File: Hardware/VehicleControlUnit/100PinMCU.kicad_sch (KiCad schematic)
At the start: 28 parts, among them J1 SWD_Header_02x02, U2 STM32G491VET6_1, Y1 Crystal

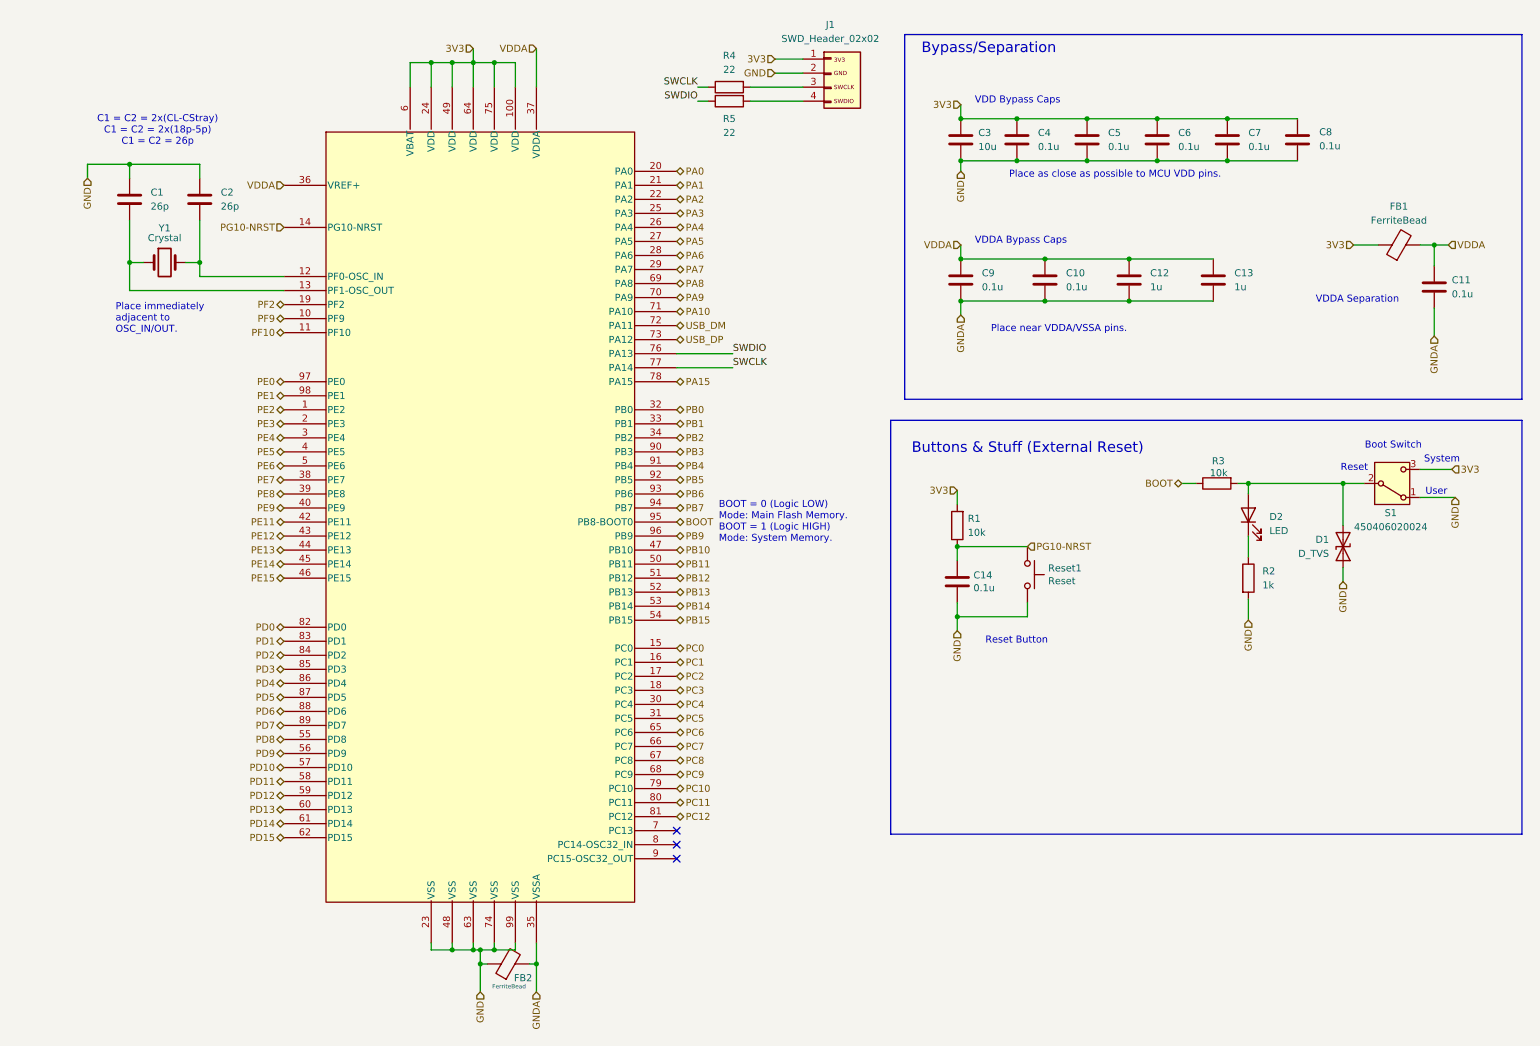
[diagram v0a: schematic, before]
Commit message: mcu pinouts todo - peripherals done
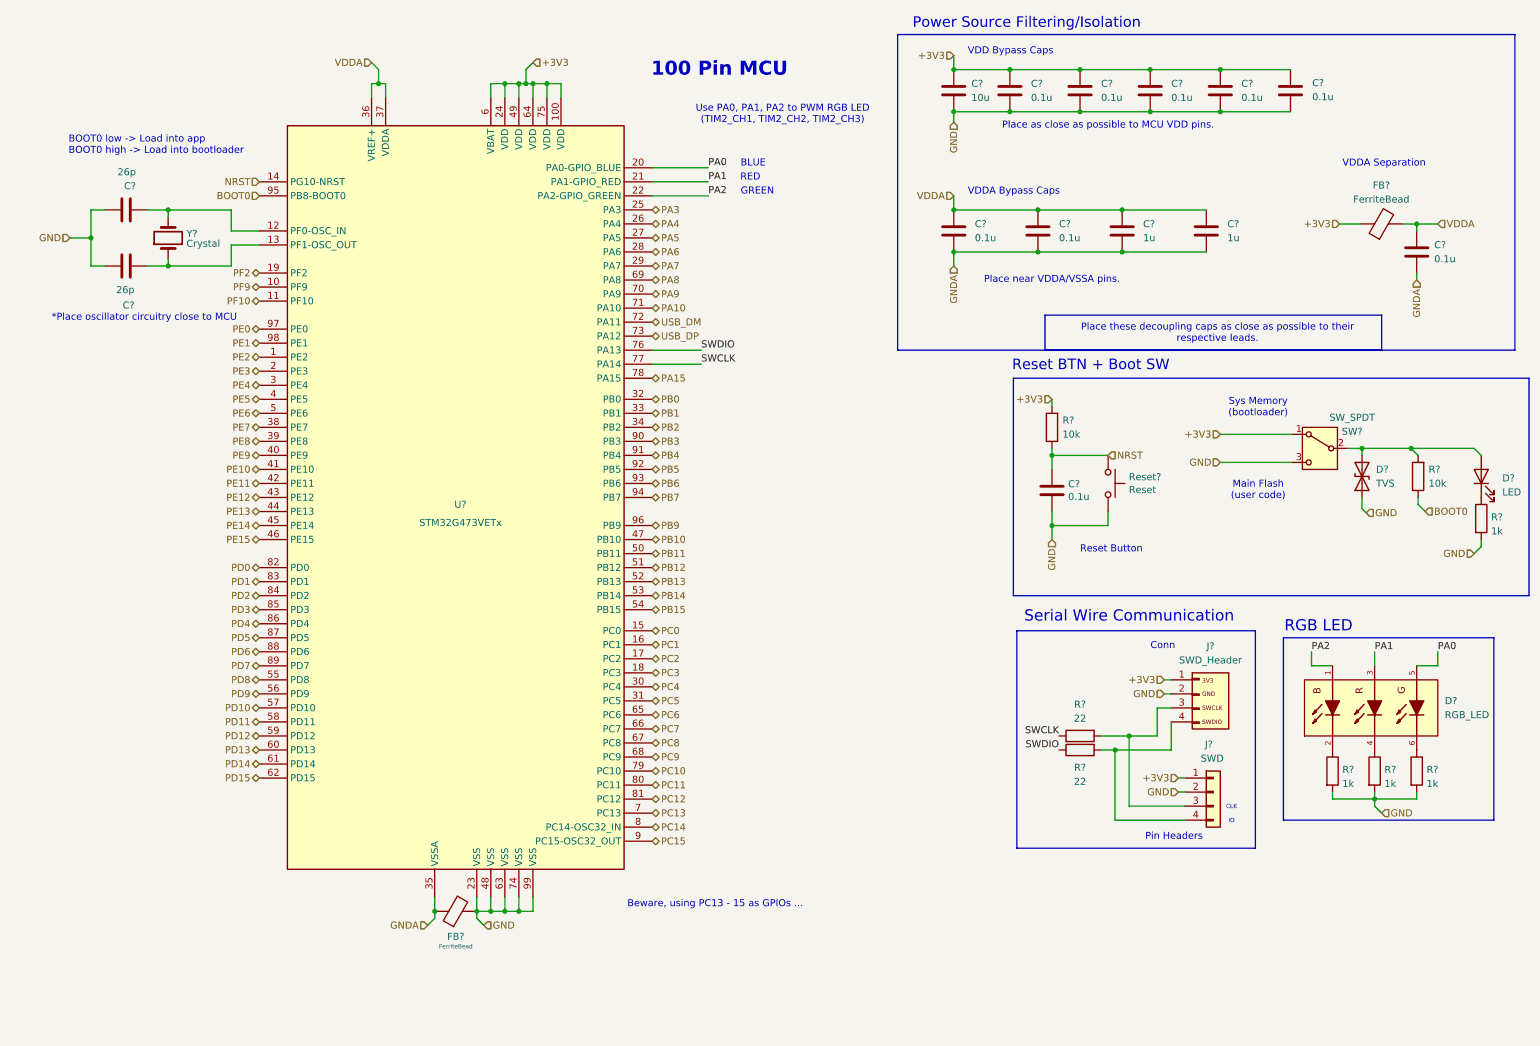
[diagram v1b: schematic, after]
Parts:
- removed C1, C2: 26p, Capacitor_SMD:C_0603_1608Metric_Pad1.08x0.95mm_HandSolder, symbol Device:C
- removed D1: D_TVS, Diode_SMD:D_SOD-323, symbol Device:D_TVS
- removed D2: LED, LED_SMD:LED_0201_0603Metric, symbol Device:LED
- removed FB2: FerriteBead, Capacitor_SMD:C_0603_1608Metric_Pad1.08x0.95mm_HandSolder, symbol Device:FerriteBead
- removed R2: 1k, Resistor_SMD:R_0603_1608Metric_Pad0.98x0.95mm_HandSolder, symbol Device:R
- removed R3: 10k, Resistor_SMD:R_0603_1608Metric_Pad0.98x0.95mm_HandSolder, symbol Device:R
- removed R4, R5: 22, Resistor_SMD:R_0603_1608Metric_Pad0.98x0.95mm_HandSolder, symbol Device:R
- removed S1: 450406020024, LHRS_Special:BootSW, symbol Switch:SW_SPDT
- removed U2: STM32G491VET6_1, LHRS_ICs:LQFP_491VET6_STM, symbol lhrs_ics:STM32G491VET6_1
- removed Y1: Crystal, LHRS_Passives:Crystal_SMD_Abracon_ABM3-2Pin_5.0x3.2mm, symbol Device:Crystal
- added C? (x2): 26p, Capacitor_SMD:C_0603_1608Metric_Pad1.08x0.95mm_HandSolder, symbol Device:C
- added D?: LED, LED_SMD:LED_0603_1608Metric, symbol lhrs_misc:Blue_LED
- added D?: TVS, Diode_SMD:D_SOD-323, symbol lhrs_misc:Boot_TVS
- added D?: RGB_LED, LHRS_Special:RGB_LED, symbol lhrs_special:RGB_LED
- added FB?: FerriteBead, Capacitor_SMD:C_0603_1608Metric_Pad1.08x0.95mm_HandSolder, symbol Device:FerriteBead
- added J?: SWD, Connector_PinHeader_2.54mm:PinHeader_1x04_P2.54mm_Vertical, symbol Connector_Generic:Conn_01x04
- added R? (x4): 1k, Resistor_SMD:R_0603_1608Metric_Pad0.98x0.95mm_HandSolder, symbol Device:R
- added R? (x2): 22, Resistor_SMD:R_0603_1608Metric_Pad0.98x0.95mm_HandSolder, symbol Device:R
- added R?: 10k, Resistor_SMD:R_0603_1608Metric_Pad0.98x0.95mm_HandSolder, symbol Device:R
- added SW?: SW_SPDT, LHRS_Special:BootSW, symbol Switch:SW_SPDT
- added U?: STM32G473VETx, LHRS_Special:100PinMCU, symbol lhrs_special:STM32G473VET6
- added Y?: Crystal, LHRS_Passives:Crystal_SMD_Abracon_ABM3-2Pin_5.0x3.2mm, symbol Device:Crystal
- J?: renamed from J1; value SWD_Header_02x02 -> SWD_Header
- renumbered C12 to C?, C10 to C?, C4 to C?, C9 to C?, C6 to C?, C7 to C?, C3 to C?, C13 to C?, C14 to C?, C11 to C?, C5 to C?, C8 to C?, FB1 to FB?, R1 to R?, Reset1 to Reset?
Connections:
- net GND: now also C?.1, C?.1, D?.1 (A1), FB?.2, J?.2 (Pin_2), R?.2, R?.2, R?.2, R?.2, SW?.3 (C), U?.23 (VSS), U?.48 (VSS), U?.63 (VSS), U?.74 (VSS), U?.99 (VSS)
- net GNDA: now also FB?.1, U?.35 (VSSA)
- net PA0: now also D?.5, U?.20 (PA0-GPIO_BLUE)
- net PA1: now also D?.3, U?.21 (PA1-GPIO_RED)
- net PA10: now also U?.71 (PA10)
- net PA15: now also U?.78 (PA15)
- net PA2: now also D?.1, U?.22 (PA2-GPIO_GREEN)
- net PA3: now also U?.25 (PA3)
- net PA4: now also U?.26 (PA4)
- net PA5: now also U?.27 (PA5)
- net PA6: now also U?.28 (PA6)
- net PA7: now also U?.29 (PA7)
- net PA8: now also U?.69 (PA8)
- net PA9: now also U?.70 (PA9)
- net PB0: now also U?.32 (PB0)
- net PB1: now also U?.33 (PB1)
- net PB10: now also U?.47 (PB10)
- net PB11: now also U?.50 (PB11)
- net PB12: now also U?.51 (PB12)
- net PB13: now also U?.52 (PB13)
- net PB14: now also U?.53 (PB14)
- net PB15: now also U?.54 (PB15)
- net PB2: now also U?.34 (PB2)
- net PB3: now also U?.90 (PB3)
- net PB4: now also U?.91 (PB4)
- net PB5: now also U?.92 (PB5)
- net PB6: now also U?.93 (PB6)
- net PB7: now also U?.94 (PB7)
- net PB9: now also U?.96 (PB9)
- net PC0: now also U?.15 (PC0)
- net PC1: now also U?.16 (PC1)
- net PC10: now also U?.79 (PC10)
- net PC11: now also U?.80 (PC11)
- net PC12: now also U?.81 (PC12)
- net PC2: now also U?.17 (PC2)
- net PC3: now also U?.18 (PC3)
- net PC4: now also U?.30 (PC4)
- net PC5: now also U?.31 (PC5)
- net PC6: now also U?.65 (PC6)
- net PC7: now also U?.66 (PC7)
- net PC8: now also U?.67 (PC8)
- net PC9: now also U?.68 (PC9)
- net PD0: now also U?.82 (PD0)
- net PD1: now also U?.83 (PD1)
- net PD10: now also U?.57 (PD10)
- net PD11: now also U?.58 (PD11)
- net PD12: now also U?.59 (PD12)
- net PD13: now also U?.60 (PD13)
- net PD14: now also U?.61 (PD14)
- net PD15: now also U?.62 (PD15)
- net PD2: now also U?.84 (PD2)
- net PD3: now also U?.85 (PD3)
- net PD4: now also U?.86 (PD4)
- net PD5: now also U?.87 (PD5)
- net PD6: now also U?.88 (PD6)
- net PD7: now also U?.89 (PD7)
- net PD8: now also U?.55 (PD8)
- net PD9: now also U?.56 (PD9)
- net PE0: now also U?.97 (PE0)
- net PE1: now also U?.98 (PE1)
- net PE11: now also U?.42 (PE11)
- net PE12: now also U?.43 (PE12)
- net PE13: now also U?.44 (PE13)
- net PE14: now also U?.45 (PE14)
- net PE15: now also U?.46 (PE15)
- net PE2: now also U?.1 (PE2)
- net PE3: now also U?.2 (PE3)
- net PE4: now also U?.3 (PE4)
- net PE5: now also U?.4 (PE5)
- net PE6: now also U?.5 (PE6)
- net PE7: now also U?.38 (PE7)
- net PE8: now also U?.39 (PE8)
- net PE9: now also U?.40 (PE9)
- net PF10: now also U?.11 (PF10)
- net PF2: now also U?.19 (PF2)
- net PF9: now also U?.10 (PF9)
- net SWCLK: now also R?.1, U?.77 (PA14)
- net SWDIO: now also R?.1, U?.76 (PA13)
- net USB_DM: now also U?.72 (PA11)
- net USB_DP: now also U?.73 (PA12)
- net VDDA: now also U?.36 (VREF+), U?.37 (VDDA)
- net at J?.3 (Pin_3): now also J?.3 (Pin_3), R?.2
- net at J?.4 (Pin_4): now also J?.4 (Pin_4), R?.2
- net 3V3 renamed +3V3
- net +3V3: now also J?.1 (Pin_1), SW?.1 (A), U?.100 (VDD), U?.24 (VDD), U?.49 (VDD), U?.6 (VBAT), U?.64 (VDD), U?.75 (VDD)
- net PG10-NRST renamed NRST
- net NRST: now also U?.14 (PG10-NRST)
- new net: D?.1 (K), R?.1
- new net: D?.2 (A), D?.2 (A2), R?.2, SW?.2 (B)
- new net: C?.2, U?.12 (PF0-OSC_IN), Y?.2
- new net: C?.2, U?.13 (PF1-OSC_OUT), Y?.1
- new net: D?.2, R?.1
- new net: D?.4, R?.1
- new net: D?.6, R?.1
- new net BOOT0: R?.1, U?.95 (PB8-BOOT0)
- new net PC13: U?.7 (PC13)
- new net PC14: U?.8 (PC14-OSC32_IN)
- new net PC15: U?.9 (PC15-OSC32_OUT)
- new net PE10: U?.41 (PE10)
- no-connect marks 3 -> 0
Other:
- note added: "*Place oscillator circuitry close to MCU"
- note added: "100 Pin MCU"
- note added: "BLUE"
- note added: "BOOT0 low -> Load into app BOOT0 high -> Load into bootloader"
- note added: "Beware, using PC13 - 15 as GPIOs ..."
- note added: "CLK"
- note added: "Conn"
- note added: "GREEN"
- note added: "IO"
- note added: "Main Flash (user code)"
- note added: "Pin Headers"
- note added: "Place these decoupling caps as close as possible to their respective leads."
- note added: "Power Source Filtering/Isolation"
- note added: "RED"
- note added: "RGB LED"
- note added: "Reset BTN + Boot SW"
- note added: "Serial Wire Communication"
- note added: "Sys Memory (bootloader)"
- note added: "Use PA0, PA1, PA2 to PWM RGB LED (TIM2_CH1, TIM2_CH2, TIM2_CH3)"
- note removed: "BOOT = 0 (Logic LOW) Mode: Main Flash Memory. BOOT = 1 (Logic HIGH) Mode: System Memory."
- note removed: "Boot Switch"
- note removed: "Buttons & Stuff (External Reset)"
- note removed: "Bypass/Separation"
- note removed: "C1 = C2 = 2x(CL-CStray) C1 = C2 = 2x(18p-5p) C1 = C2 = 26p"
- note removed: "Place immediately adjacent to OSC_IN/OUT."
- note removed: "Reset"
- note removed: "System"
- note removed: "User"
- moved on the sheet: C?, FB?, J?, R?, Reset?

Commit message: VCU more like diddle-u, mika time
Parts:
- gave numbers to parts that had none: 33

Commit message: ughhhhhhhhhhhhhhhhhhh VCU will lokwey explode and propell the car
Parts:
- renumbered J5 to J7, J6 to J8, R11 to R15, R12 to R16, R13 to R17, R14 to R18, R15 to R19, R16 to R20, R17 to R21, R18 to R22
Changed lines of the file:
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@@
 		(dnp no)
 		(fields_autoplaced yes)
-		(property "Reference" "R11"
+		(property "Reference" "R15"
 			(at 198.755 87.6299 0)
 			(show_name no)
@@
 			(project "VehicleControlUnit"
 				(path "/e864fac9-3897-46c9-9101-6d5488c6cd3a/f9087b5b-32fd-4bb7-84dd-9fe64614d383/e8918db0-ed0e-4663-8139-dd25306e146c"
-					(reference "R11")
+					(reference "R15")
 					(unit 1)
 				)
@@
 		(in_pos_files yes)
 		(dnp no)
-		(property "Reference" "R18"
+		(property "Reference" "R22"
 			(at 276.352 105.156 0)
 			(show_name no)
@@
 			(project "VehicleControlUnit"
 				(path "/e864fac9-3897-46c9-9101-6d5488c6cd3a/f9087b5b-32fd-4bb7-84dd-9fe64614d383/e8918db0-ed0e-4663-8139-dd25306e146c"
-					(reference "R18")
+					(reference "R22")
 					(unit 1)
 				)
@@
 		(in_pos_files yes)
 		(dnp no)
-		(property "Reference" "R13"
+		(property "Reference" "R17"
 			(at 201.93 150.495 90)
 			(show_name no)
@@
 			(project "VehicleControlUnit"
 				(path "/e864fac9-3897-46c9-9101-6d5488c6cd3a/f9087b5b-32fd-4bb7-84dd-9fe64614d383/e8918db0-ed0e-4663-8139-dd25306e146c"
-					(reference "R13")
+					(reference "R17")
 					(unit 1)
 				)
@@
 		(in_pos_files yes)
 		(dnp no)
-		(property "Reference" "J5"
+		(property "Reference" "J7"
 			(at 225.552 128.524 0)
 			(show_name no)
@@
 			(project "VehicleControlUnit"
 				(path "/e864fac9-3897-46c9-9101-6d5488c6cd3a/f9087b5b-32fd-4bb7-84dd-9fe64614d383/e8918db0-ed0e-4663-8139-dd25306e146c"
-					(reference "J5")
+					(reference "J7")
 					(unit 1)
 				)
@@
 		(in_pos_files yes)
 		(dnp no)
-		(property "Reference" "R15"
+		(property "Reference" "R19"
 			(at 257.048 150.876 0)
 			(show_name no)
@@
 			(project "VehicleControlUnit"
 				(path "/e864fac9-3897-46c9-9101-6d5488c6cd3a/f9087b5b-32fd-4bb7-84dd-9fe64614d383/e8918db0-ed0e-4663-8139-dd25306e146c"
-					(reference "R15")
+					(reference "R19")
 					(unit 1)
 				)
@@
 		(in_pos_files yes)
 		(dnp no)
-		(property "Reference" "R14"
+		(property "Reference" "R18"
 			(at 249.428 150.876 0)
 			(show_name no)
@@
 			(project "VehicleControlUnit"
 				(path "/e864fac9-3897-46c9-9101-6d5488c6cd3a/f9087b5b-32fd-4bb7-84dd-9fe64614d383/e8918db0-ed0e-4663-8139-dd25306e146c"
-					(reference "R14")
+					(reference "R18")
 					(unit 1)
 				)
@@
 		(in_pos_files yes)
 		(dnp no)
-		(property "Reference" "R17"
+		(property "Reference" "R21"
 			(at 265.049 96.5199 0)
 			(show_name no)
@@
 			(project "VehicleControlUnit"
 				(path "/e864fac9-3897-46c9-9101-6d5488c6cd3a/f9087b5b-32fd-4bb7-84dd-9fe64614d383/e8918db0-ed0e-4663-8139-dd25306e146c"
-					(reference "R17")
+					(reference "R21")
 					(unit 1)
 				)
@@
 		(in_pos_files yes)
 		(dnp no)
-		(property "Reference" "R16"
+		(property "Reference" "R20"
 			(at 264.668 150.876 0)
 			(show_name no)
@@
 			(project "VehicleControlUnit"
 				(path "/e864fac9-3897-46c9-9101-6d5488c6cd3a/f9087b5b-32fd-4bb7-84dd-9fe64614d383/e8918db0-ed0e-4663-8139-dd25306e146c"
-					(reference "R16")
+					(reference "R20")
 					(unit 1)
 				)
@@
 		(dnp no)
 		(fields_autoplaced yes)
-		(property "Reference" "R12"
+		(property "Reference" "R16"
 			(at 201.93 139.065 90)
 			(show_name no)
@@
 			(project "VehicleControlUnit"
 				(path "/e864fac9-3897-46c9-9101-6d5488c6cd3a/f9087b5b-32fd-4bb7-84dd-9fe64614d383/e8918db0-ed0e-4663-8139-dd25306e146c"
-					(reference "R12")
+					(reference "R16")
 					(unit 1)
 				)
@@
 		(in_pos_files yes)
 		(dnp no)
-		(property "Reference" "J6"
+		(property "Reference" "J8"
 			(at 224.536 146.304 0)
 			(show_name no)
@@
 			(project "VehicleControlUnit"
 				(path "/e864fac9-3897-46c9-9101-6d5488c6cd3a/f9087b5b-32fd-4bb7-84dd-9fe64614d383/e8918db0-ed0e-4663-8139-dd25306e146c"
-					(reference "J6")
+					(reference "J8")
 					(unit 1)
 				)
